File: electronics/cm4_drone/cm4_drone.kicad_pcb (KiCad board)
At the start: 4 copper layers, 69.2 x 40 mm, 55 parts, among them J8 Conn_01x02_Female, J9 Conn_01x02_Female, U1 74LVC1G04, U3 ADS1115IDGS, U5 Compute_Module_4_Connectors

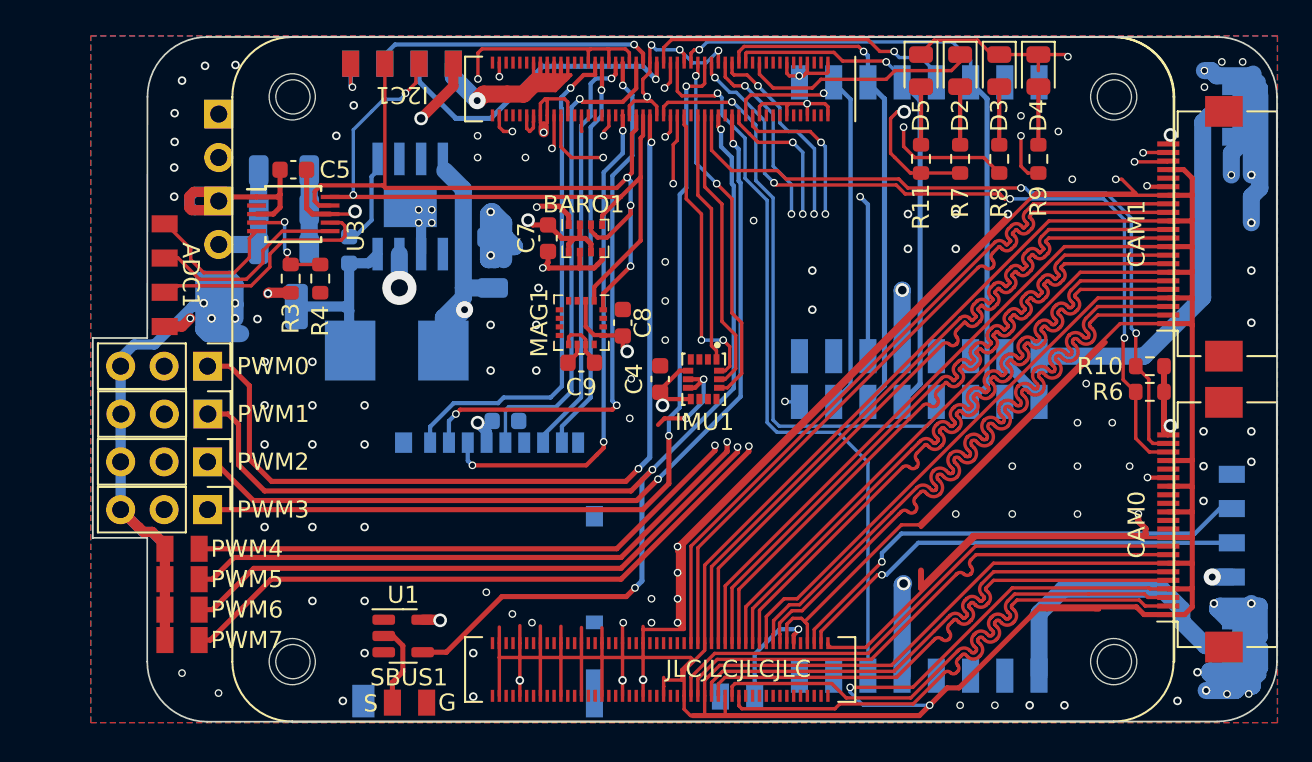
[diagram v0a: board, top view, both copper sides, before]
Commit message: new CM4 carrier board
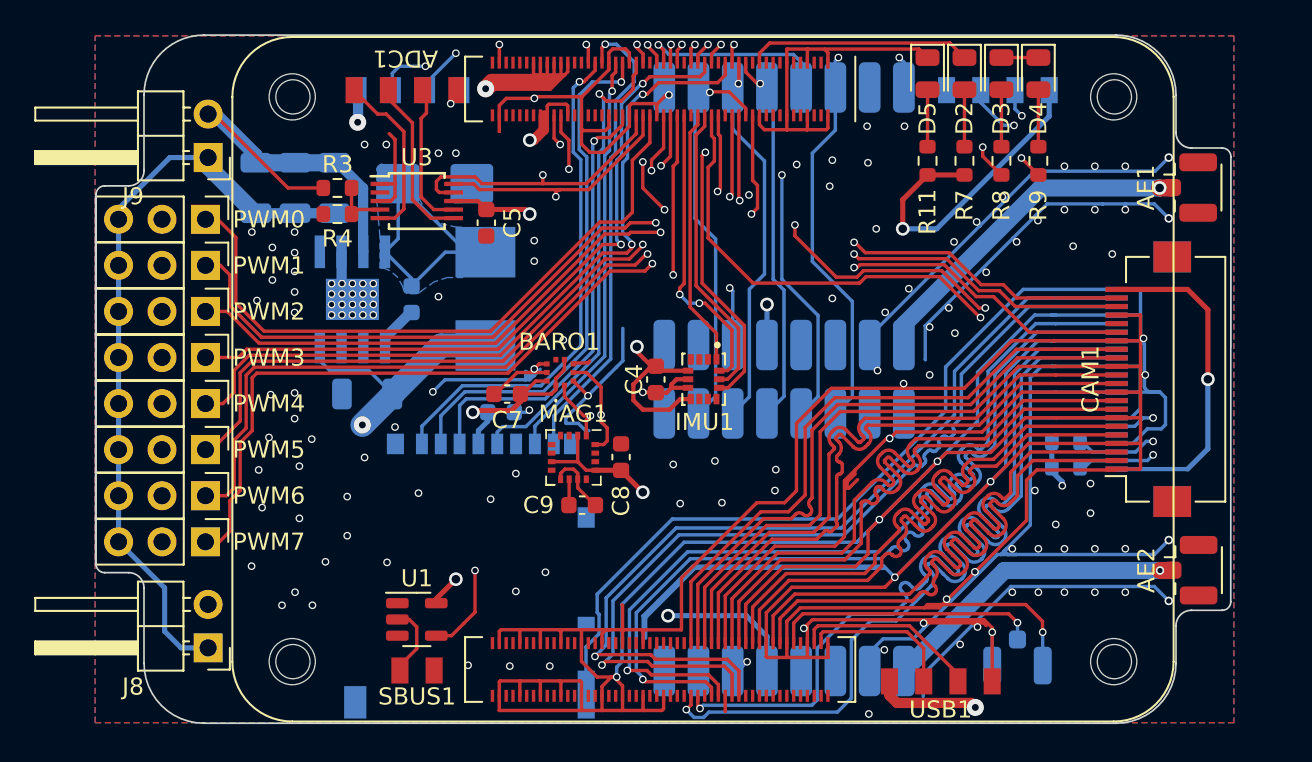
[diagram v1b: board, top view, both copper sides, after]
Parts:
- AE1, AE2, J8, J9, USB1: moved to F.Cu
- BARO1: value BMP280 -> BMP581; footprint Package_LGA:Bosch_LGA-8_2x2.5mm_P0.65mm_ClockwisePinNumbering -> footprints:BMP581
- CAM0, I2C1, R10, R6: moved to B.Cu
- D1: value V5PA22-M3/I -> SL54-3G; footprint Diode_SMD:D_2010_5025Metric -> Diode_SMD:D_SMB
- L1: value SRP0615-100K -> SRP6030VA-100M
- PWM4, PWM5, PWM6, PWM7: value Conn_01x02_Female -> Conn_01x03_Female; footprint cm4_drone:Breakout_1x02_2mm_SMD -> Connector_PinHeader_2.54mm:PinHeader_1x03_P2.54mm_Vertical
- TV1: footprint cm4_drone:Breakout_1x02_2mm_SMD -> Connector_Coaxial:U.FL_Hirose_U.FL-R-SMT-1_Vertical
- moved I2C1 34.9 mm to (17.2, -16.9)
- moved J8 31.2 mm to (-29.0, 15.7)
- moved USB1 19.3 mm to (13.9, 17.7), turned to 0 degrees
- moved ADC1 17.7 mm to (-17.4, -16.9), turned to 0 degrees
- moved TV1 16.5 mm to (18.3, 16.3), turned to -90 degrees
- moved D1 12.6 mm to (-15.7, -11.4), turned to 0 degrees
- moved C5 11.7 mm to (-12.7, -9.14), turned to 90 degrees
- moved C6 10.6 mm to (-19.7, 0.86), turned to 180 degrees
- moved C7 9.41 mm to (-11.5, 0.86), turned to 180 degrees
- moved CAM1 9.02 mm to (26.0, -0.00)
- moved CAM0 9.02 mm to (26.0, 0.00), turned to -90 degrees
- moved PWM3 8.89 mm to (-29.1, -1.27)
- moved PWM2 8.79 mm to (-29.1, -3.96)
- moved PWM1 8.69 mm to (-29.1, -6.65)
- moved PWM4 8.59 mm to (-29.1, 1.42), turned to -90 degrees
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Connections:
- net Net-(C3-Pad1) renamed /DC-SW
- BARO1 pad 1: GND -> CM4_3.3V
- BARO1 pad 2: CM4_3.3V -> I2C1_SCL
- BARO1 pad 3: I2C1_SDA -> GND
- BARO1 pad 4: I2C1_SCL -> I2C1_SDA
- BARO1 pad 7: GND -> unconnected-(BARO1-INT-Pad7)
- BARO1 pad 8: CM4_3.3V -> GND
- MAG1 pad 7: unconnected-(MAG1-Pad7) -> CM4_3.3V
- PWM4 pad 2: GND -> unconnected-(PWM4-Pin_2-Pad2)
- PWM5 pad 2: GND -> unconnected-(PWM5-Pin_2-Pad2)
- PWM6 pad 2: GND -> unconnected-(PWM6-Pin_2-Pad2)
- PWM7 pad 2: GND -> unconnected-(PWM7-Pin_2-Pad2)
- TV1 pad 1: GND -> TVOUT
- TV1 pad 2: TVOUT -> GND
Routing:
- net CM4_3.3V: track 56.8 -> 103.9 mm, vias 13 -> 11
- net I2C1_SDA: track 43.8 -> 74.7 mm
- net GND: track 744.4 -> 715.6 mm, vias 131 -> 146
- net I2C1_SCL: track 42.7 -> 67.8 mm, vias 2 -> 3
- net CAM0_D0_N: track 32.0 -> 52.6 mm, vias 0 -> 1
- net CAM0_D1_N: track 32.0 -> 52.5 mm, vias 0 -> 1
- net CAM0_D0_P: track 32.0 -> 52.4 mm, vias 0 -> 1
- net CAM0_D1_P: track 32.0 -> 52.4 mm, vias 0 -> 1
- net CAM0_CK_P: track 32.2 -> 52.4 mm, vias 0 -> 1
- net CAM0_CK_N: track 32.1 -> 52.3 mm, vias 0 -> 1
- net USB2_D-: track 26.8 -> 8.92 mm, vias 1 -> 0
- net 5V: track 132.2 -> 149.9 mm, vias 3 -> 4
- net USB2_D+: track 28.4 -> 10.9 mm, vias 1 -> 0
- net PI_PWM1: track 58.2 -> 43.9 mm, vias 3 -> 2
- net PI_PWM0: track 59.2 -> 45.2 mm, vias 3 -> 2
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- added copper zone on B.Cu, net /DC-SW
- added copper zone on In1.Cu, net GND
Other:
- board size 69.2 x 40 mm -> 66.3 x 40.2 mm
- board text removed: "5V"
- board text removed: "D+"
- board text removed: "D-"
- board text removed: "G"
- board text removed: "JLCJLCJLCJLC"
- board text removed: "S"

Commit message: electronics: fix labels shapes
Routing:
- net GND: vias 146 -> 145
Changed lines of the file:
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@@
   (via (at -26.1 -4.6) (size 0.45) (drill 0.3) (layers "F.Cu" "B.Cu") (free) (net 1))
   (via (at -25.2 -7.7) (size 0.45) (drill 0.3) (layers "F.Cu" "B.Cu") (free) (net 1))
-  (via (at 10.0838 -8.7884) (size 0.45) (drill 0.3) (layers "F.Cu" "B.Cu") (free) (net 1))
   (via (at -20.828 6.858) (size 0.45) (drill 0.3) (layers "F.Cu" "B.Cu") (free) (net 1))
   (via (at 24.638 -9.906) (size 0.45) (drill 0.3) (layers "F.Cu" "B.Cu") (net 1))
@@
   (segment (start 7.62 -6.096) (end 3.048 -6.096) (width 0.2) (layer "In1.Cu") (net 7))
   (segment (start 3.048 -6.096) (end -1.524 -10.668) (width 0.2) (layer "In1.Cu") (net 7))
-  (segment (start 8.890264 -6.4262) (end 14.0716 -6.4262) (width 0.2) (layer "In1.Cu") (net 7))
   (segment (start -9.144 -12.7) (end -10.414 -12.7) (width 0.2) (layer "In1.Cu") (net 7))
-  (segment (start 15.6464 -4.8514) (end 18.6436 -4.8514) (width 0.2) (layer "In1.Cu") (net 7))
   (segment (start -1.524 -10.668) (end -7.112 -10.668) (width 0.2) (layer "In1.Cu") (net 7))
-  (segment (start 18.6436 -4.8514) (end 25.7556 2.2606) (width 0.2) (layer "In1.Cu") (net 7))
   (segment (start 8.0518 -6.5278) (end 7.62 -6.096) (width 0.2) (layer "In1.Cu") (net 7))
   (segment (start -7.112 -10.668) (end -9.144 -12.7) (width 0.2) (layer "In1.Cu") (net 7))
-  (segment (start 8.788664 -6.5278) (end 8.890264 -6.4262) (width 0.2) (layer "In1.Cu") (net 7))
-  (segment (start 25.7556 2.2606) (end 26.2636 2.2606) (width 0.2) (layer "In1.Cu") (net 7))
   (segment (start -10.414 -12.7) (end -11.938 -14.224) (width 0.2) (layer "In1.Cu") (net 7))
-  (segment (start 14.0716 -6.4262) (end 15.6464 -4.8514) (width 0.2) (layer "In1.Cu") (net 7))
   (segment (start 8.788664 -6.5278) (end 8.0518 -6.5278) (width 0.2) (layer "In1.Cu") (net 7))
   (segment (start -11.938 -14.224) (end -11.938 -19.558) (width 0.2) (layer "In1.Cu") (net 7))
+  (segment (start 25.2476 2.2606) (end 17.653 -5.334) (width 0.2) (layer "In2.Cu") (net 7))
+  (segment (start 26.2636 2.2606) (end 25.2476 2.2606) (width 0.2) (layer "In2.Cu") (net 7))
+  (segment (start 14.986 -5.334) (end 13.7922 -6.5278) (width 0.2) (layer "In2.Cu") (net 7))
+  (segment (start 17.653 -5.334) (end 14.986 -5.334) (width 0.2) (layer "In2.Cu") (net 7))
+  (segment (start 13.7922 -6.5278) (end 8.788664 -6.5278) (width 0.2) (layer "In2.Cu") (net 7))
   (segment (start 26.2636 2.2606) (end 25.6794 2.2606) (width 0.2) (layer "B.Cu") (net 7))
   (segment (start 25.189107 2.750893) (end 24.129999 2.750893) (width 0.2) (layer "B.Cu") (net 7))

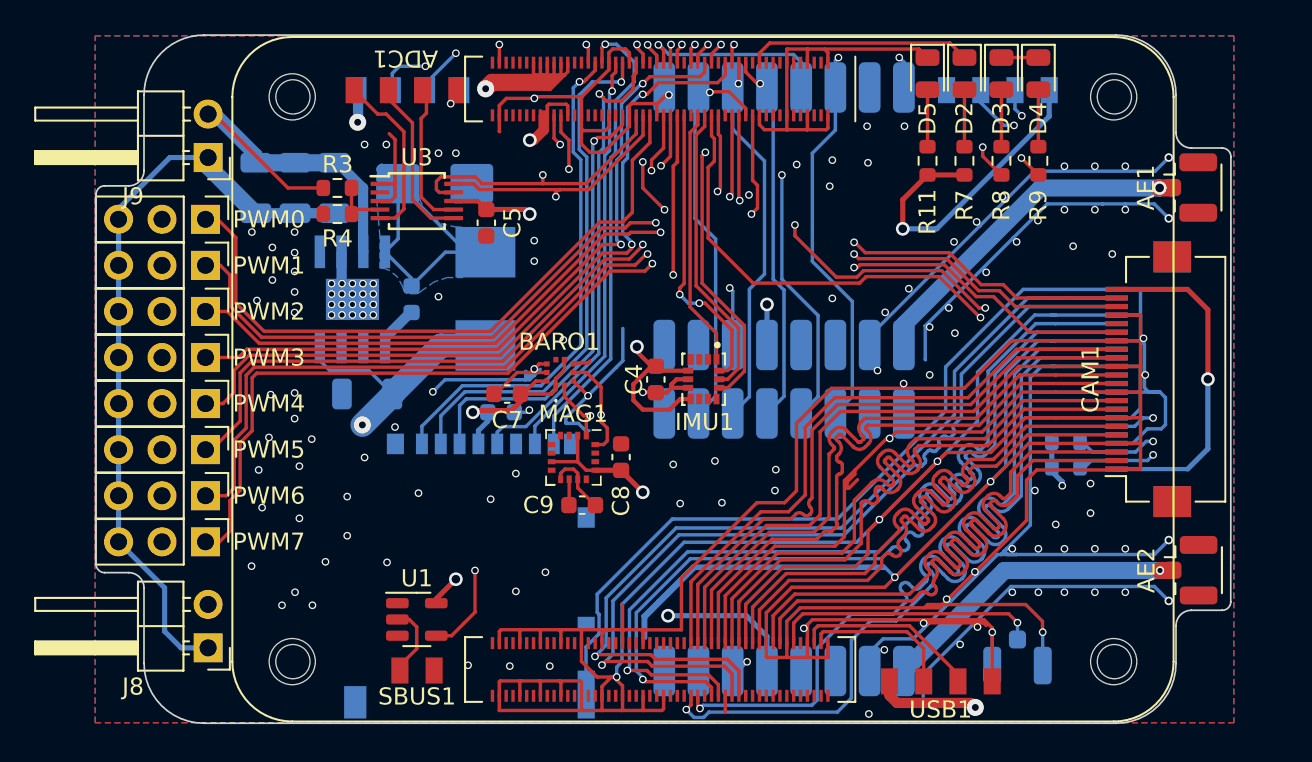
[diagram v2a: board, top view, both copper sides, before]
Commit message: fix for issue #14
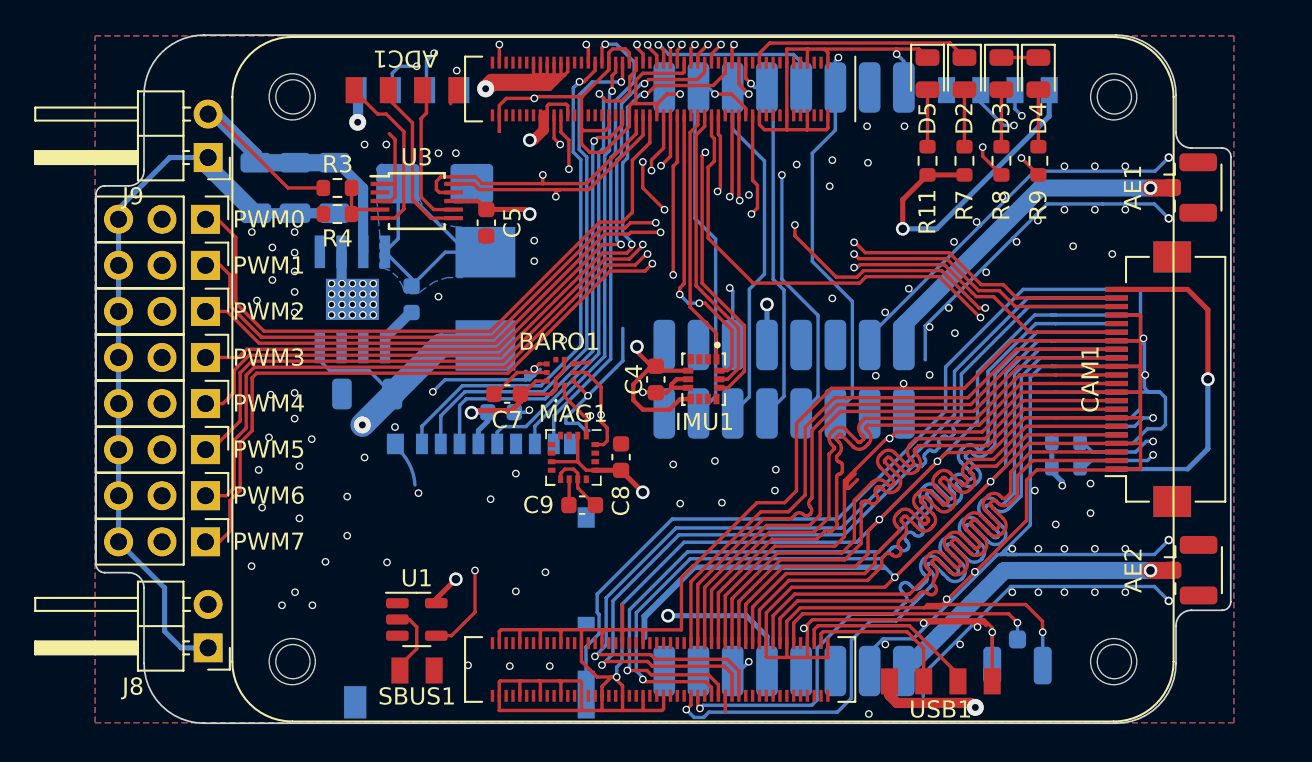
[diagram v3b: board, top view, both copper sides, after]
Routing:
- net GND: track 715.6 -> 722.0 mm
- net CM4_3.3V: track 103.9 -> 107.4 mm
- net RF_MOSI: track 22.3 -> 23.8 mm
- net UART0_TX: track 14.9 -> 15.6 mm

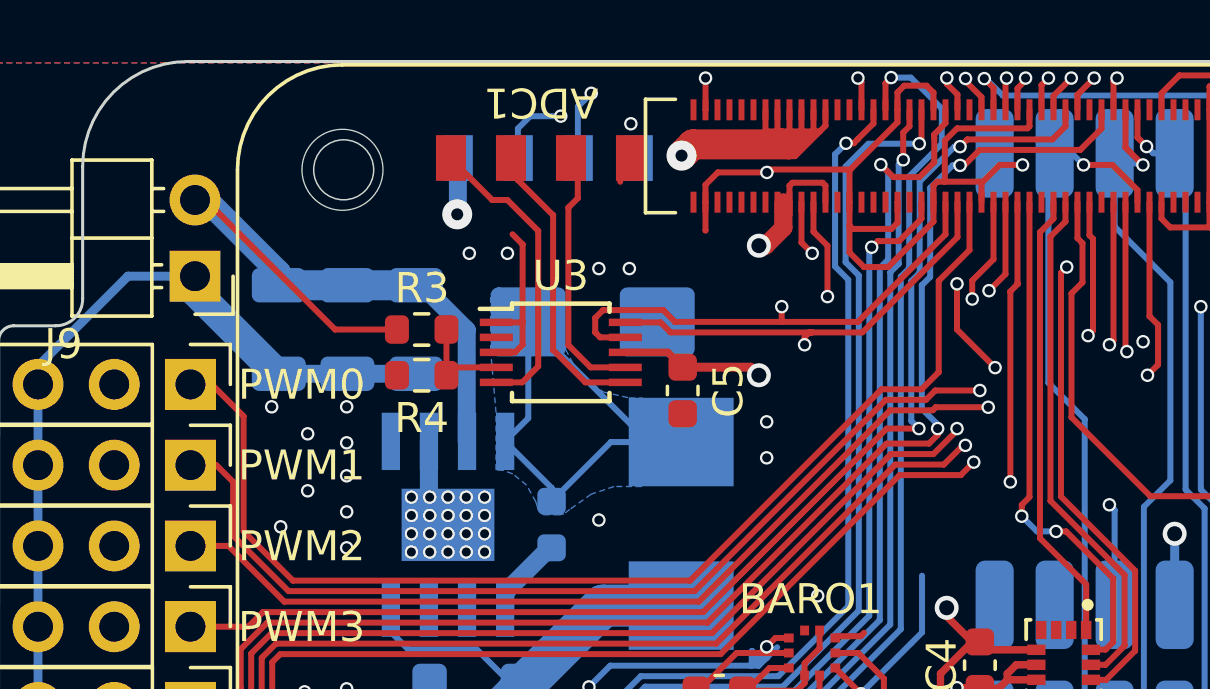
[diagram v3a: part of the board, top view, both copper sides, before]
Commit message: electronics: add TVS diode to prevent battery spikes from frying voltage regulator
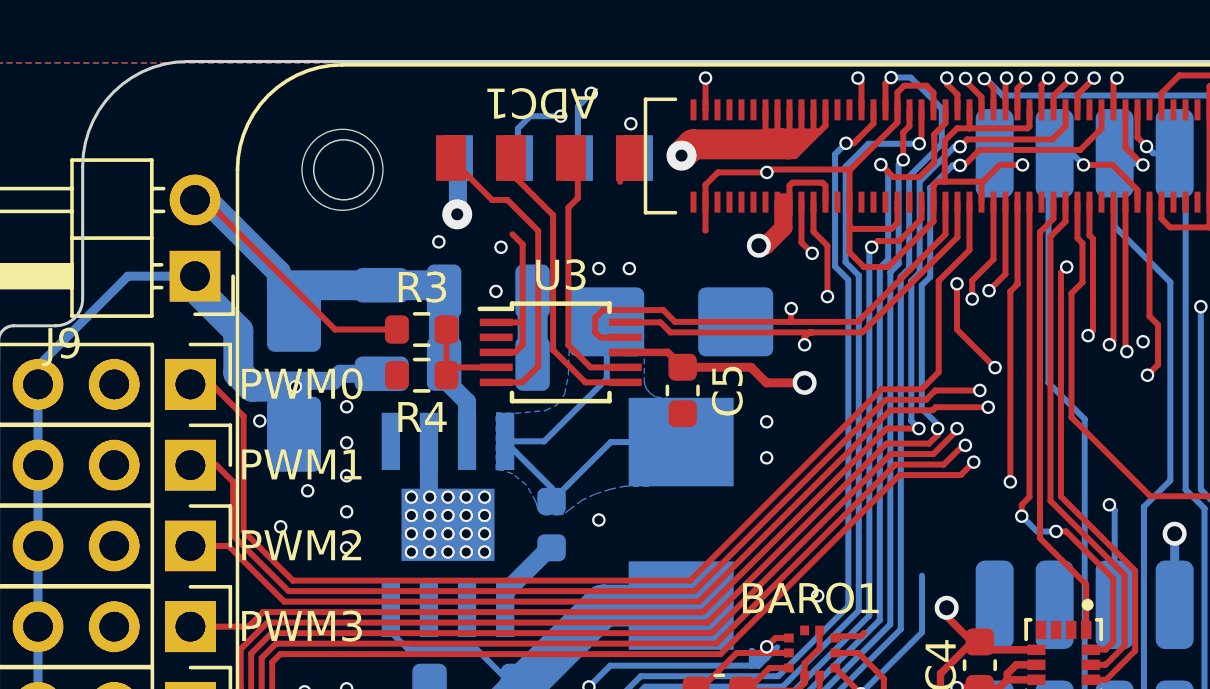
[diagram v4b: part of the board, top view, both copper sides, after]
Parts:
- added D6: SMAJ36A, Diode_SMD:D_SMA, B.Cu at (-25.7, -9.68)
- moved C2 7.10 mm to (-19.2, -12.4), turned to 0 degrees
- moved C13 2.67 mm to (-19.2, -10.0), turned to 0 degrees
- moved D1 2.62 mm to (-13.1, -11.4)
- moved C12 1.14 mm to (-22.7, -11.2)
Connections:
- net /DC-SW renamed Net-(D1-K)
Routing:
- net GND: track 722.0 -> 726.1 mm, vias 145 -> 146
- net Net-(D1-K): track 18.8 -> 15.0 mm
- net CM4_3.3V: track 107.4 -> 109.0 mm
- net I2C1_SDA: track 74.7 -> 74.0 mm
